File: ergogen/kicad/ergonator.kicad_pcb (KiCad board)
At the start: 2 copper layers, 121.2 x 110.9 mm, 38 parts

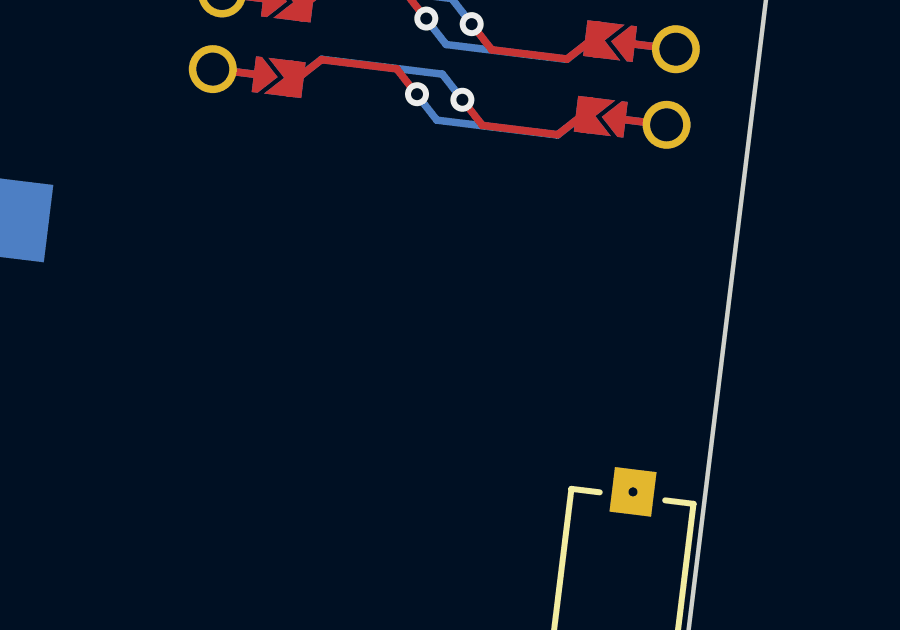
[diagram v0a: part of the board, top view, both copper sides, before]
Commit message: Added TRRS connector and changed row and column net.
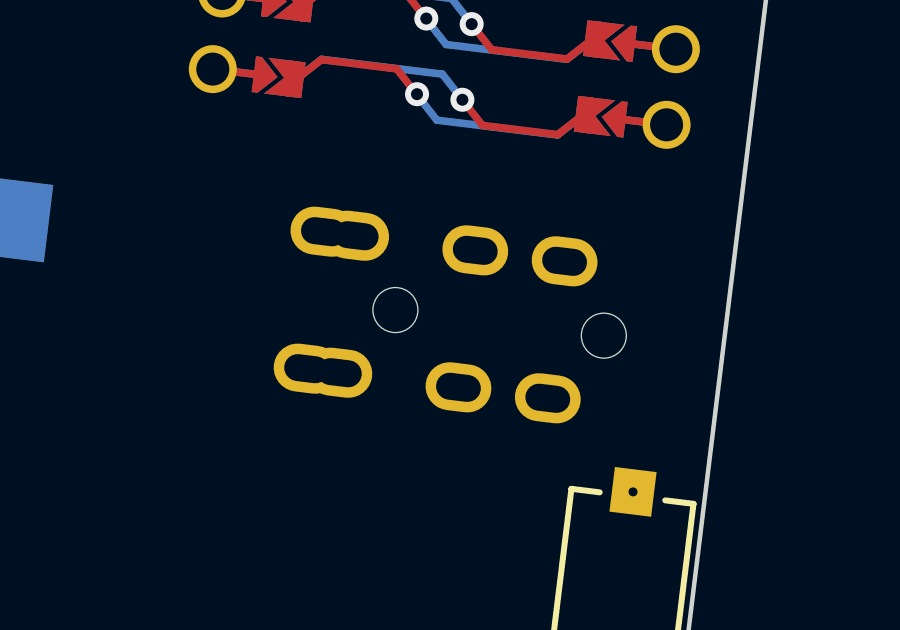
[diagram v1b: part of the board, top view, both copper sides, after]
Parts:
- added TRRS1: TRRS-PJ-320A-dual, TRRS-PJ-320A-dual, F.Cu at (203.3, 110.3)
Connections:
- D1 pad 1: P2 -> P4
- D10 pad 1: P2 -> P4
- D13 pad 1: P2 -> P4
- D16 pad 1: P8 -> P10
- D17 pad 1: P8 -> P10
- D18 pad 1: P8 -> P10
- D4 pad 1: P2 -> P4
- D7 pad 1: P2 -> P4
- S1 pad 1: P7 -> P9
- S10 pad 1: P4 -> P6
- S11 pad 1: P4 -> P6
- S12 pad 1: P4 -> P6
- S13 pad 1: P3 -> P5
- S14 pad 1: P3 -> P5
- S15 pad 1: P3 -> P5
- S16 pad 1: P5 -> P7
- S17 pad 1: P4 -> P6
- S18 pad 1: P3 -> P5
- S2 pad 1: P7 -> P9
- S3 pad 1: P7 -> P9
- S4 pad 1: P6 -> P8
- S5 pad 1: P6 -> P8
- S6 pad 1: P6 -> P8
- S7 pad 1: P5 -> P7
- S8 pad 1: P5 -> P7
- S9 pad 1: P5 -> P7

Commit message: Wiring done.
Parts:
- D1, D10, D11, D12, D13, D14, D15, D16, D17, D18, D2, D3, D4, D5, D6, D7, D8, D9: moved to F.Cu
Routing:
- net (no net): track 262.1 -> 0.00 mm
- net P9: track 0.00 -> 205.6 mm
- net P6: track 0.00 -> 169.4 mm
- net P5: track 0.00 -> 155.4 mm
- net P7: track 0.00 -> 145.4 mm, vias 1 -> 2
- net P0: track 0.00 -> 138.6 mm
- net P8: track 0.00 -> 136.0 mm, vias 1 -> 3
- net P4: track 0.00 -> 134.4 mm
- net P1: track 0.00 -> 120.4 mm
- net P10: track 0.00 -> 113.8 mm
- net GND: track 0.00 -> 85.5 mm
- net RST: track 0.00 -> 59.5 mm
- net P2: track 0.00 -> 54.4 mm
- net VCC: track 0.00 -> 52.0 mm
- net P3: track 0.00 -> 49.7 mm
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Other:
- net class Default removed

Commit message: Added version number on the board and started work so silkscreen art.
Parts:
- D1, D10, D11, D12, D13, D14, D15, D16, D17, D18, D2, D3, D4, D5, D6, D7, D8, D9: moved to 
- moved D5 9.32 mm to (121.4, 87.7), turned to -7 degrees
- moved D14 9.32 mm to (174.7, 96.7), turned to -7 degrees
- moved D13 9.32 mm to (172.7, 113.6), turned to -7 degrees
- moved D10 9.32 mm to (155.1, 108.9), turned to -7 degrees
- moved D6 9.32 mm to (123.5, 70.8), turned to -7 degrees
- moved D9 9.32 mm to (141.7, 70.5), turned to -7 degrees
- moved D1 9.32 mm to (100.0, 107.0), turned to 0 degrees
- moved D2 9.32 mm to (100.0, 90.0), turned to 0 degrees
- moved D3 9.32 mm to (100.0, 73.0), turned to 0 degrees
- moved D15 9.32 mm to (176.8, 79.9), turned to -7 degrees
- moved D12 9.32 mm to (159.2, 75.2), turned to -7 degrees
- moved D18 9.32 mm to (178.4, 154.1), turned to -48 degrees
- moved D17 9.32 mm to (164.4, 142.7), turned to -30 degrees
- moved D11 9.32 mm to (157.2, 92.1), turned to -7 degrees
- moved D8 9.32 mm to (139.6, 87.4), turned to -7 degrees
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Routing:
- net (no net): track 0.00 -> 262.1 mm
- net P9: track 205.6 -> 0.00 mm
- net P6: track 169.4 -> 0.00 mm
- net P5: track 155.4 -> 0.00 mm
- net P7: track 145.4 -> 0.00 mm, vias 2 -> 1
- net P0: track 138.6 -> 0.00 mm
- net P8: track 136.0 -> 0.00 mm, vias 3 -> 1
- net P4: track 134.4 -> 0.00 mm
- net P1: track 120.4 -> 0.00 mm
- net P10: track 113.8 -> 0.00 mm
- net GND: track 85.5 -> 0.00 mm
- net RST: track 59.5 -> 0.00 mm
- net P2: track 54.4 -> 0.00 mm
- net VCC: track 52.0 -> 0.00 mm
- net P3: track 49.7 -> 0.00 mm
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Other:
- net class Default added: clearance 0.2, trace_width 0.25, via_dia 0.8, via_drill 0.4
- board text added: "ERGONATOR[v1.0]"
- board text removed: "Ergonator"

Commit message: Ergontaor[v1.0] with correct switches and complete wiring.
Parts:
- added _10: , MountingHole_2.2mm_M2_Pad_Via, F.Cu at (191.0, 102.1)
- added _7: , MountingHole_2.2mm_M2_Pad_Via, F.Cu at (119.2, 51.9)
- added _8: , MountingHole_2.2mm_M2_Pad_Via, F.Cu at (121.5, 86.8)
- added _9: , MountingHole_2.2mm_M2_Pad_Via, F.Cu at (195.2, 53.7)
- D1, D10, D11, D12, D13, D14, D15, D16, D17, D18, D2, D3, D4, D5, D6, D7, D8, D9: moved to F.Cu
- moved S18 28.9 mm to (200.4, 125.9), turned to -41 degrees
- moved D18 28.8 mm to (195.8, 131.2), turned to -41 degrees
- moved TRRS1 28.2 mm to (215.2, 84.7), turned to -90 degrees
- moved S19 26.7 mm to (210.2, 90.7), turned to 0 degrees
- moved D17 26.6 mm to (180.5, 121.6), turned to -23 degrees
- moved S17 26.4 mm to (183.3, 115.2), turned to -23 degrees
- moved MCU1 26.4 mm to (207.2, 61.2), turned to -90 degrees
- moved D13 25.2 mm to (185.2, 91.7), turned to 0 degrees
- moved S13 24.9 mm to (185.2, 84.7), turned to 0 degrees
- moved D16 24.5 mm to (163.0, 117.2), turned to -5 degrees
- moved D14 24.4 mm to (185.2, 74.7), turned to 0 degrees
- moved S16 24.1 mm to (163.6, 110.2), turned to -5 degrees
- moved S14 24.1 mm to (185.2, 67.7), turned to 0 degrees
- moved D15 23.7 mm to (185.2, 57.7), turned to 0 degrees
- moved S15 23.4 mm to (185.2, 50.7), turned to 0 degrees
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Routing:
- net (no net): track 262.1 -> 0.00 mm
- net P9: track 0.00 -> 227.2 mm, vias 1 -> 4
- net P7: track 0.00 -> 216.8 mm, vias 1 -> 5
- net P6: track 0.00 -> 197.9 mm, vias 1 -> 5
- net P8: track 0.00 -> 194.2 mm, vias 1 -> 4
- net P5: track 0.00 -> 149.7 mm, vias 1 -> 6
- net P4: track 0.00 -> 137.9 mm
- net P0: track 0.00 -> 132.0 mm
- net P10: track 0.00 -> 125.7 mm
- net P1: track 0.00 -> 119.0 mm
- net GND: track 0.00 -> 74.8 mm
- net P2: track 0.00 -> 58.0 mm
- net RST: track 0.00 -> 56.9 mm
- net P3: track 0.00 -> 56.7 mm
- net VCC: track 0.00 -> 53.7 mm
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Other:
- board size 121.2 x 110.9 mm -> 122.1 x 104.5 mm
- net class Default removed

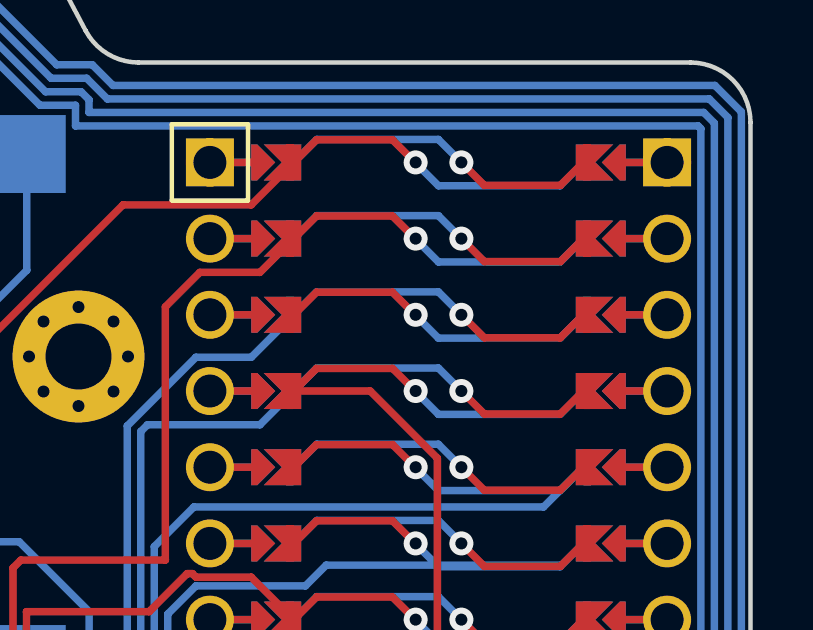
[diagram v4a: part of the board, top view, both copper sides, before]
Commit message: Connected grounds on pcb.
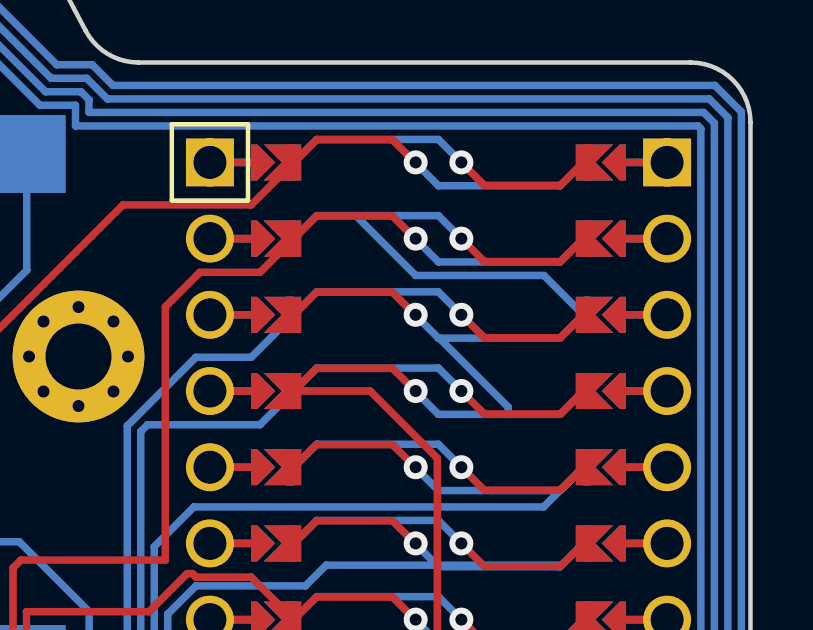
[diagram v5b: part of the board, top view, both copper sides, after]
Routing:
- net GND: track 74.8 -> 87.2 mm
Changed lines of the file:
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@@
   (via (at 206.462867 54.874657) (size 0.8) (drill 0.4) (layers "F.Cu" "B.Cu") (net 29))
   (via (at 207.986867 49.794657) (size 0.8) (drill 0.4) (layers "F.Cu" "B.Cu") (net 29))
+  (segment (start 212.050867 52.334657) (end 210.739088 51.022878) (width 0.25) (layer "B.Cu") (net 29))
+  (segment (start 207.222966 55.652878) (end 209.55 55.652878) (width 0.25) (layer "B.Cu") (net 29))
   (segment (start 207.986867 49.794657) (end 207.220867 49.028657) (width 0.25) (layer "B.Cu") (net 29))
-  (segment (start 207.222966 55.652878) (end 211.278966 55.652878) (width 0.25) (layer "B.Cu") (net 29))
   (segment (start 207.222966 53.112878) (end 211.278966 53.112878) (width 0.25) (layer "B.Cu") (net 29))
-  (segment (start 207.220867 49.028657) (end 203.164867 49.028657) (width 0.25) (layer "B.Cu") (net 29))
+  (segment (start 207.250393 53.112878) (end 209.55 55.412485) (width 0.25) (layer "B.Cu") (net 29))
   (segment (start 203.164867 49.028657) (end 202.398867 49.794657) (width 0.25) (layer "B.Cu") (net 29))
   (segment (start 206.456966 52.346878) (end 207.222966 53.112878) (width 0.25) (layer "B.Cu") (net 29))
+  (segment (start 204.47 49.028657) (end 203.164867 49.028657) (width 0.25) (layer "B.Cu") (net 29))
   (segment (start 211.278966 55.652878) (end 212.044966 54.886878) (width 0.25) (layer "B.Cu") (net 29))
+  (segment (start 206.464221 51.022878) (end 204.47 49.028657) (width 0.25) (layer "B.Cu") (net 29))
+  (segment (start 210.739088 51.022878) (end 206.464221 51.022878) (width 0.25) (layer "B.Cu") (net 29))
+  (segment (start 209.55 55.652878) (end 211.278966 55.652878) (width 0.25) (layer "B.Cu") (net 29))
+  (segment (start 207.222966 53.112878) (end 207.250393 53.112878) (width 0.25) (layer "B.Cu") (net 29))
   (segment (start 206.456966 54.886878) (end 207.222966 55.652878) (width 0.25) (layer "B.Cu") (net 29))
+  (segment (start 209.55 55.412485) (end 209.55 55.652878) (width 0.25) (layer "B.Cu") (net 29))
   (segment (start 211.278966 53.112878) (end 212.044966 52.346878) (width 0.25) (layer "B.Cu") (net 29))
+  (segment (start 207.220867 49.028657) (end 204.47 49.028657) (width 0.25) (layer "B.Cu") (net 29))
   (segment (start 207.986867 52.334657) (end 208.752867 53.100657) (width 0.25) (layer "F.Cu") (net 30))
   (segment (start 208.752867 53.100657) (end 211.284867 53.100657) (width 0.25) (layer "F.Cu") (net 30))

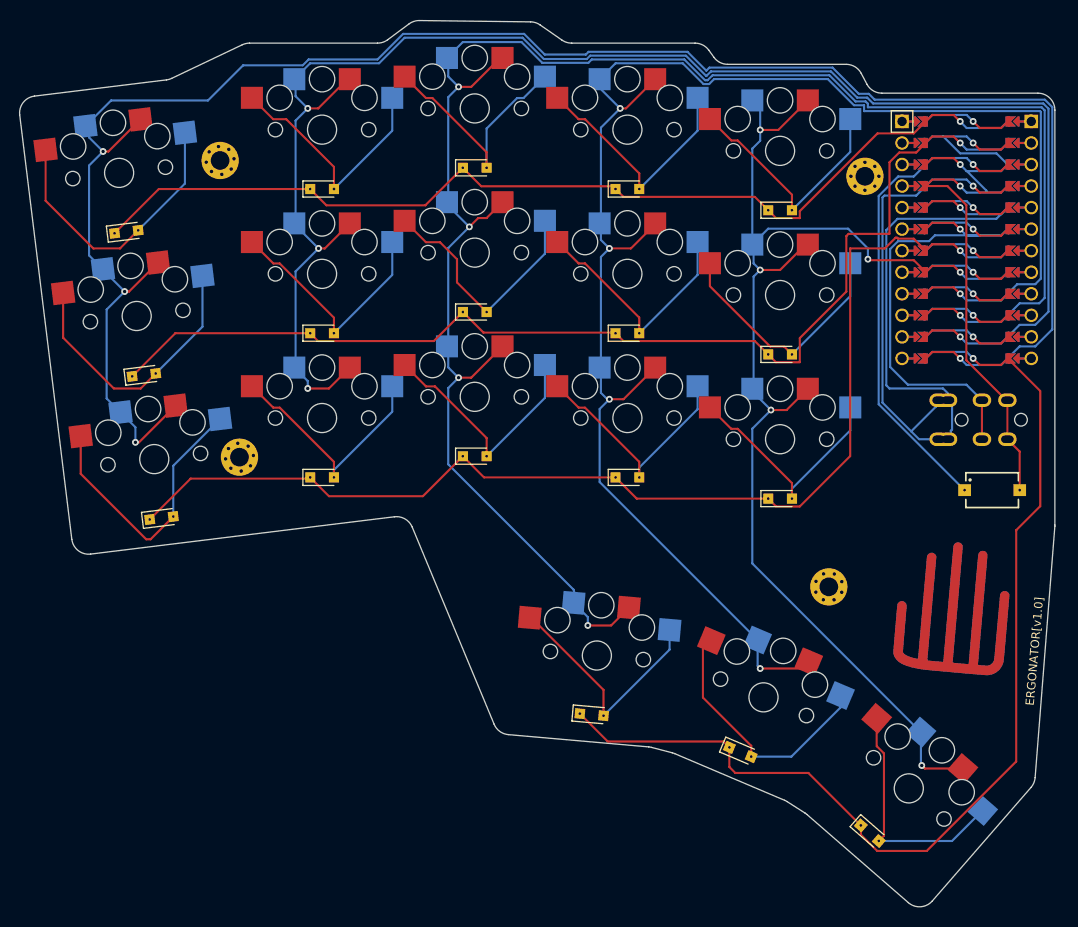
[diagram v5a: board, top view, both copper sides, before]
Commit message: Changed trrs connector footprint and started modifying config for a case.
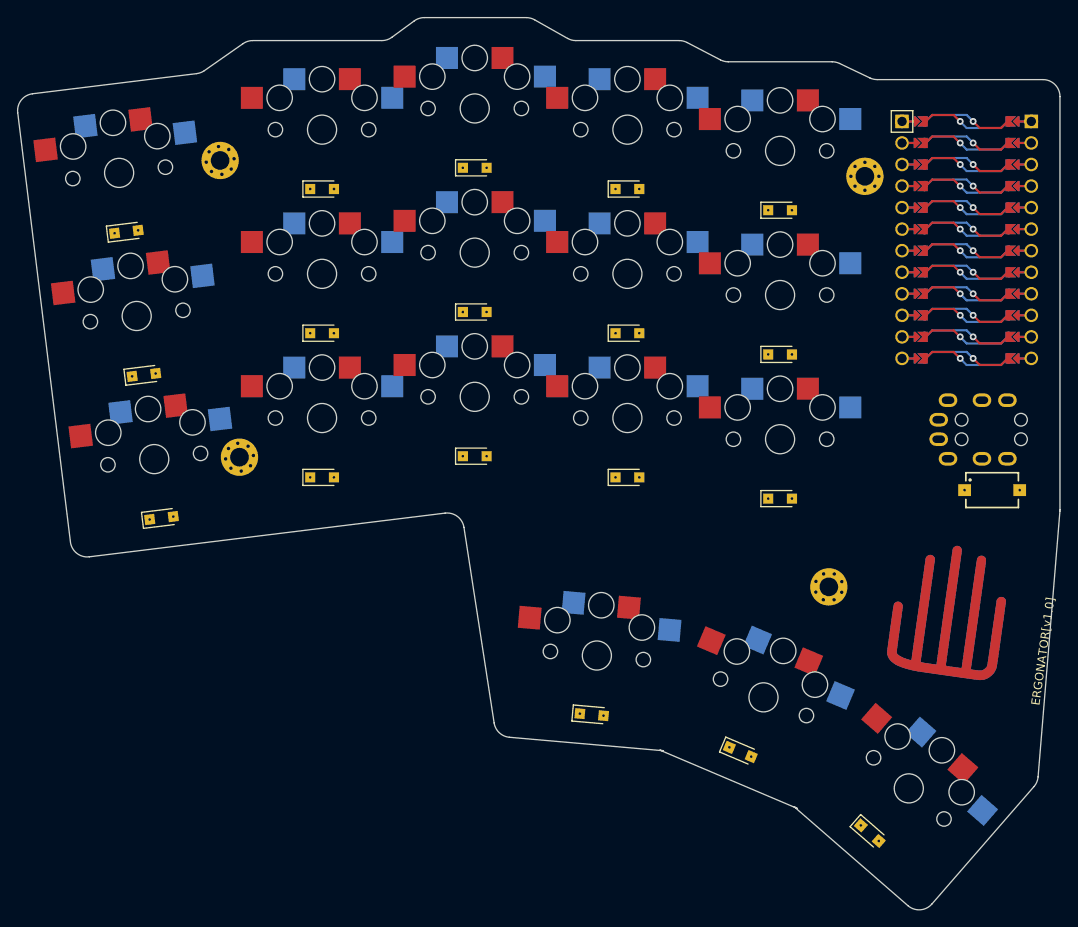
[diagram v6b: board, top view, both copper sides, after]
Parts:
- D1, D10, D11, D12, D13, D14, D15, D16, D17, D18, D2, D3, D4, D5, D6, D7, D8, D9: moved to 
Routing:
- net (no net): track 0.00 -> 262.1 mm
- net P9: track 227.2 -> 0.00 mm, vias 4 -> 1
- net P7: track 216.8 -> 0.00 mm, vias 5 -> 1
- net P6: track 197.9 -> 0.00 mm, vias 5 -> 1
- net P8: track 194.2 -> 0.00 mm, vias 4 -> 1
- net P5: track 149.7 -> 0.00 mm, vias 6 -> 1
- net P4: track 137.9 -> 0.00 mm
- net P0: track 132.0 -> 0.00 mm
- net P10: track 125.7 -> 0.00 mm
- net P1: track 119.0 -> 0.00 mm
- net GND: track 87.2 -> 0.00 mm
- net P2: track 58.0 -> 0.00 mm
- net RST: track 56.9 -> 0.00 mm
- net P3: track 56.7 -> 0.00 mm
- net VCC: track 53.7 -> 0.00 mm
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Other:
- board size 122.1 x 104.5 mm -> 122.9 x 105.2 mm
- net class Default added: clearance 0.2, trace_width 0.25, via_dia 0.8, via_drill 0.4
